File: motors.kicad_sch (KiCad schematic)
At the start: 5 parts, among them J11 Conn_01x03, J12 Conn_01x03, J13 Conn_01x03, J14 Conn_01x03, J15 Conn_01x03

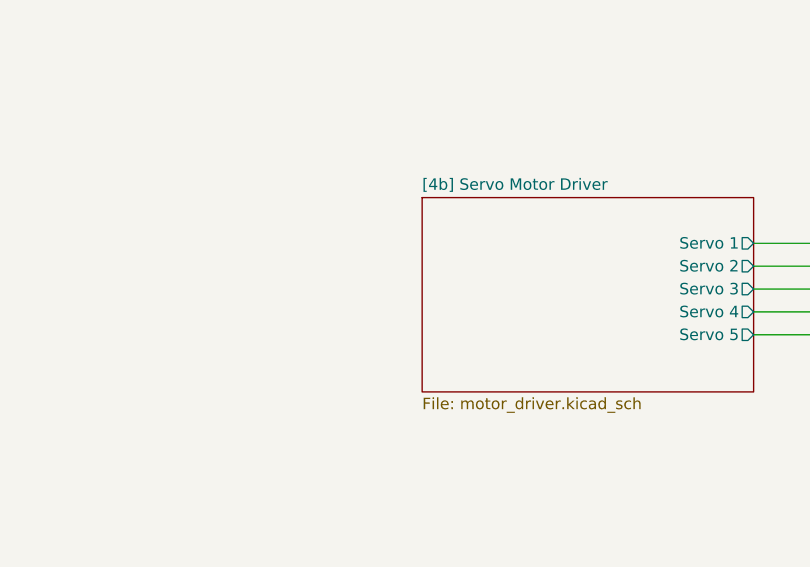
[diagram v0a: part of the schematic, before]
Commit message: feat(pcb): made the fan controlled by a NPN transistor
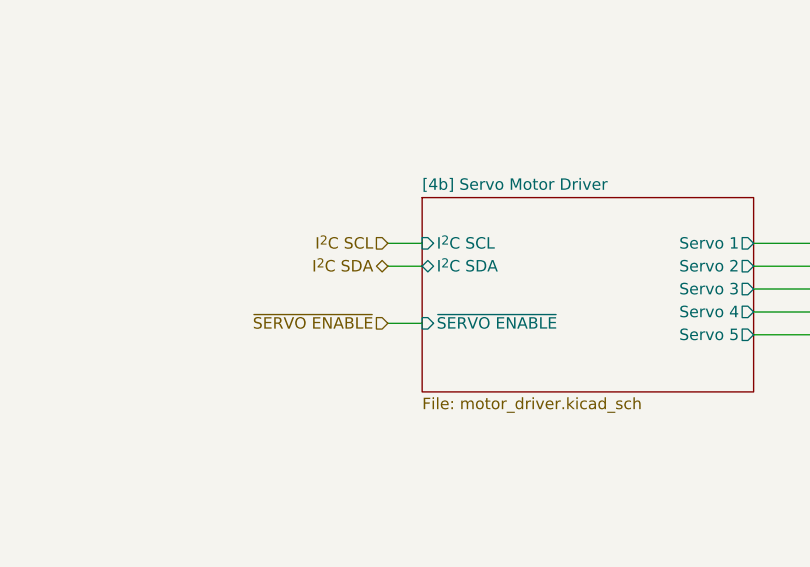
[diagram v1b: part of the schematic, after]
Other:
- sheet [4b] Servo Motor Driver ports: added I^{2}C SCL, I^{2}C SDA, ~{SERVO ENABLE}; removed none
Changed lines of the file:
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@@
+	(wire
+		(pts
+			(xy 165.1 80.01) (xy 168.91 80.01)
+		)
+		(stroke
+			(width 0)
+			(type default)
+		)
+	)
 	(wire
 		(pts
@@
 	(wire
 		(pts
+			(xy 165.1 82.55) (xy 168.91 82.55)
+		)
+		(stroke
+			(width 0)
+			(type default)
+		)
+	)
+	(wire
+		(pts
 			(xy 212.09 90.17) (xy 212.09 115.57)
 		)
@@
 		(pts
 			(xy 224.79 95.25) (xy 224.79 104.14)
+		)
+		(stroke
+			(width 0)
+			(type default)
+		)
+	)
+	(wire
+		(pts
+			(xy 165.1 88.9) (xy 168.91 88.9)
 		)
 		(stroke
@@
 		)
 	)
+	(hierarchical_label "I^{2}C SDA"
+		(shape bidirectional)
+		(at 165.1 82.55 180)
+		(effects
+			(font
+				(size 1.27 1.27)
+			)
+			(justify right)
+		)
+	)
 	(hierarchical_label "M2DB"
 		(shape input)
@@
 		)
 	)
+	(hierarchical_label "I^{2}C SCL"
+		(shape input)
+		(at 165.1 80.01 180)
+		(effects
+			(font
+				(size 1.27 1.27)
+			)
+			(justify right)
+		)
+	)
 	(hierarchical_label "M3DB"
 		(shape input)
@@
 		)
 	)
+	(hierarchical_label "~{SERVO ENABLE}"
+		(shape input)
+		(at 165.1 88.9 180)
+		(effects
+			(font
+				(size 1.27 1.27)
+			)
+			(justify right)
+		)
+	)
 	(rule_area
 		(polyline
 			(pts
-				(xy 247.65 67.31) (xy 166.37 67.31) (xy 166.37 128.27) (xy 247.65 128.27)
+				(xy 247.65 67.31) (xy 137.16 67.31) (xy 137.16 128.27) (xy 247.65 128.27)
 			)
 			(stroke
@@
 			)
 		)
+		(pin "I^{2}C SCL" input
+			(at 168.91 80.01 180)
+			(effects
+				(font
+					(size 1.27 1.27)
+				)
+				(justify left)
+			)
+		)
+		(pin "I^{2}C SDA" bidirectional
+			(at 168.91 82.55 180)
+			(effects
+				(font
+					(size 1.27 1.27)
+				)
+				(justify left)
+			)
+		)
+		(pin "~{SERVO ENABLE}" input
+			(at 168.91 88.9 180)
+			(effects
+				(font
+					(size 1.27 1.27)
+				)
+				(justify left)
+			)
+		)

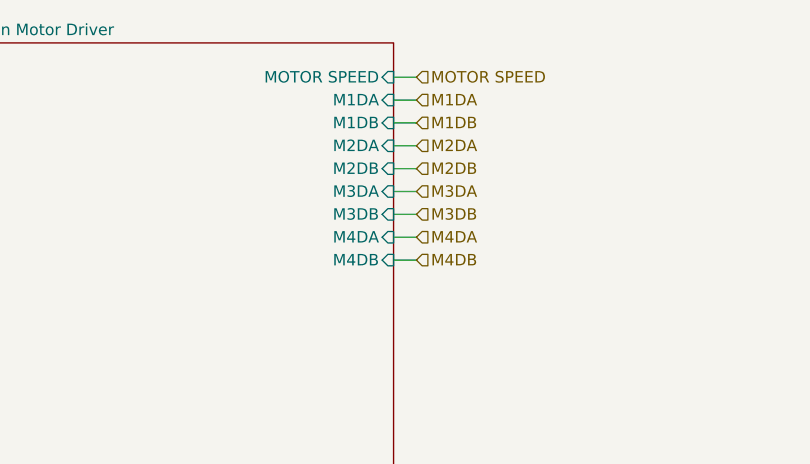
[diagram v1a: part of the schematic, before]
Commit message: doc(pcb): added docs for some of the main components of the HAT
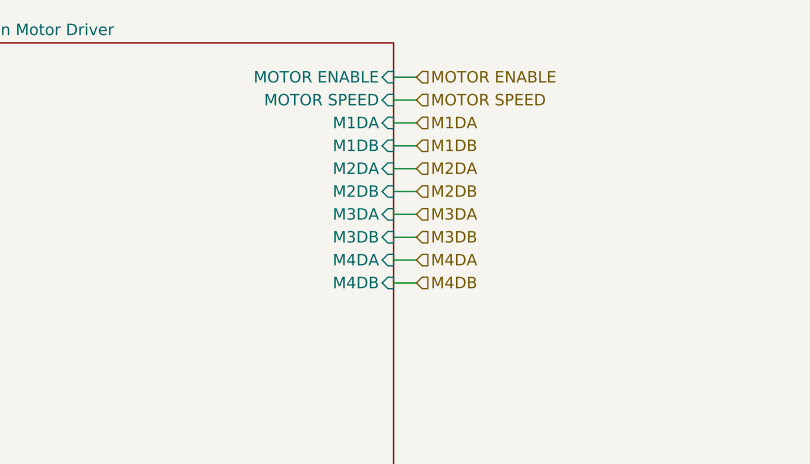
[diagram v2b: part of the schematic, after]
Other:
- sheet [4a] Main Motor Driver ports: added MOTOR ENABLE; removed none

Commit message: feat(pcb): (somewhat) finalized all the parts needed
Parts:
- J11, J12, J13, J14, J15: footprint (none) -> Connector_PinHeader_2.54mm:PinHeader_1x03_P2.54mm_Vertical
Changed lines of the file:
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@@
 			)
 		)
-		(property "Footprint" ""
+		(property "Footprint" "Connector_PinHeader_2.54mm:PinHeader_1x03_P2.54mm_Vertical"
 			(at 232.41 106.68 0)
 			(effects
@@
 			)
 		)
-		(property "Footprint" ""
+		(property "Footprint" "Connector_PinHeader_2.54mm:PinHeader_1x03_P2.54mm_Vertical"
 			(at 232.41 115.57 0)
 			(effects
@@
 			)
 		)
-		(property "Footprint" ""
+		(property "Footprint" "Connector_PinHeader_2.54mm:PinHeader_1x03_P2.54mm_Vertical"
 			(at 232.41 80.01 0)
 			(effects
@@
 			)
 		)
-		(property "Footprint" ""
+		(property "Footprint" "Connector_PinHeader_2.54mm:PinHeader_1x03_P2.54mm_Vertical"
 			(at 232.41 97.79 0)
 			(effects
@@
 			)
 		)
-		(property "Footprint" ""
+		(property "Footprint" "Connector_PinHeader_2.54mm:PinHeader_1x03_P2.54mm_Vertical"
 			(at 232.41 88.9 0)
 			(effects

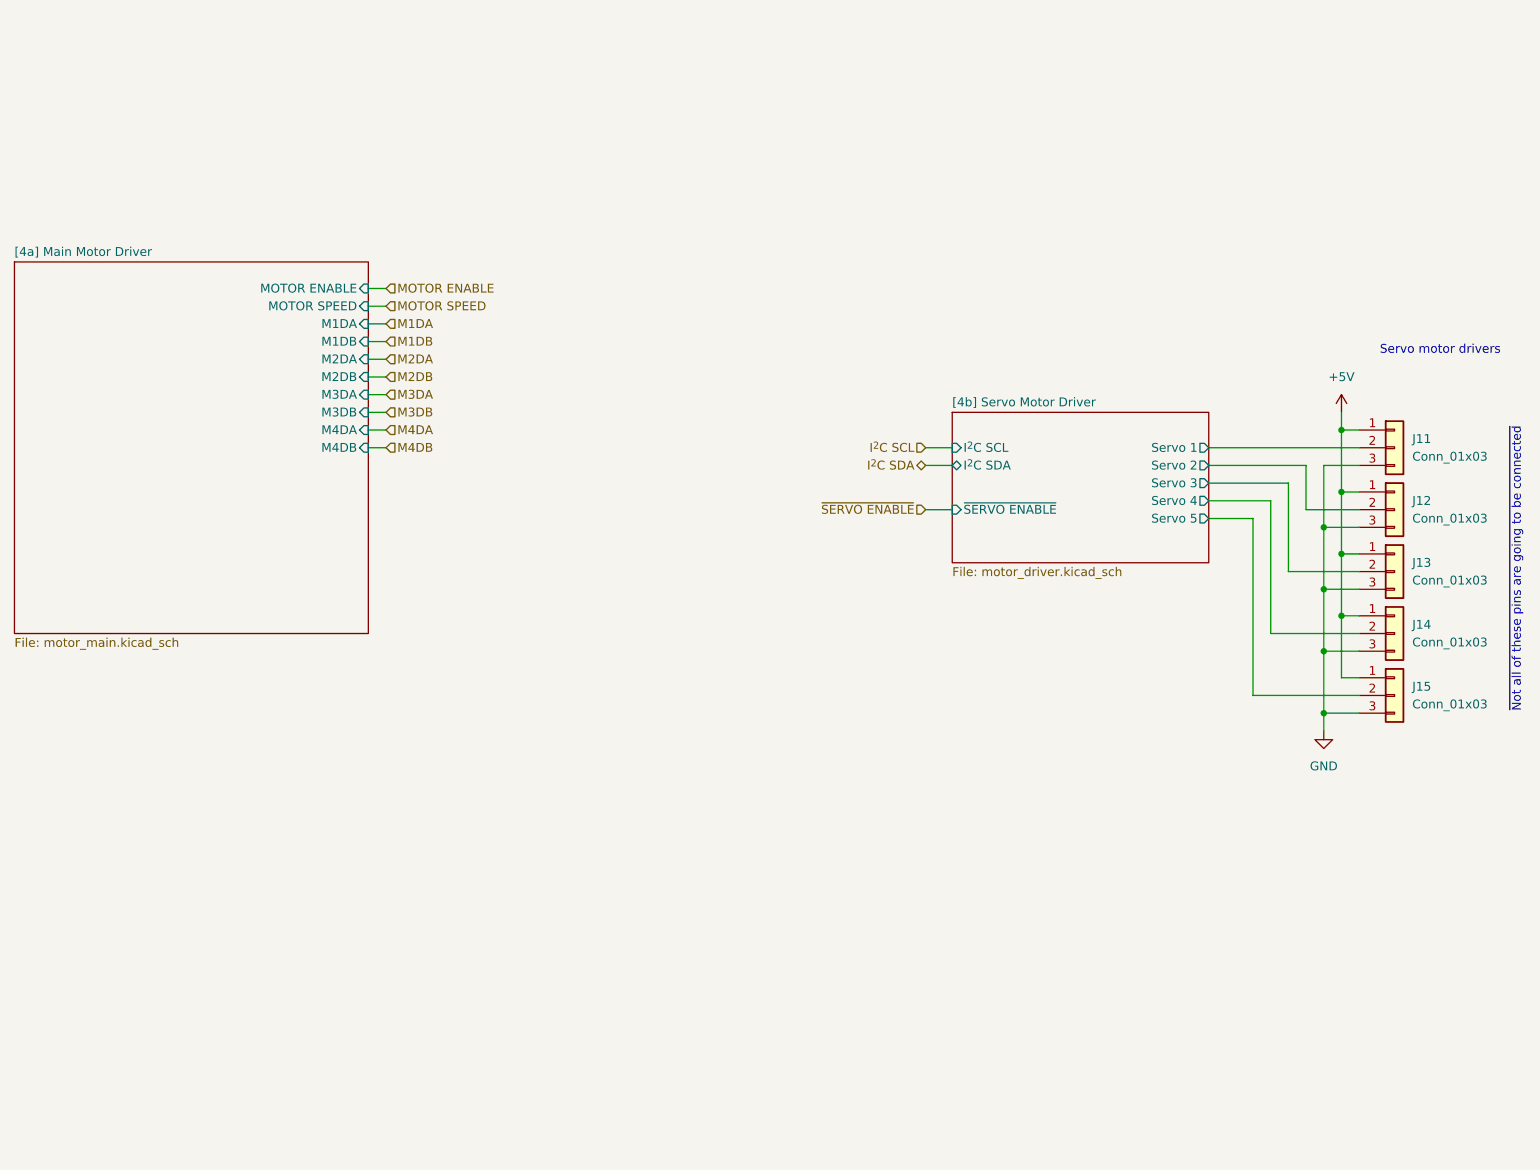
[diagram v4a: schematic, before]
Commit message: feat: removed servo motors
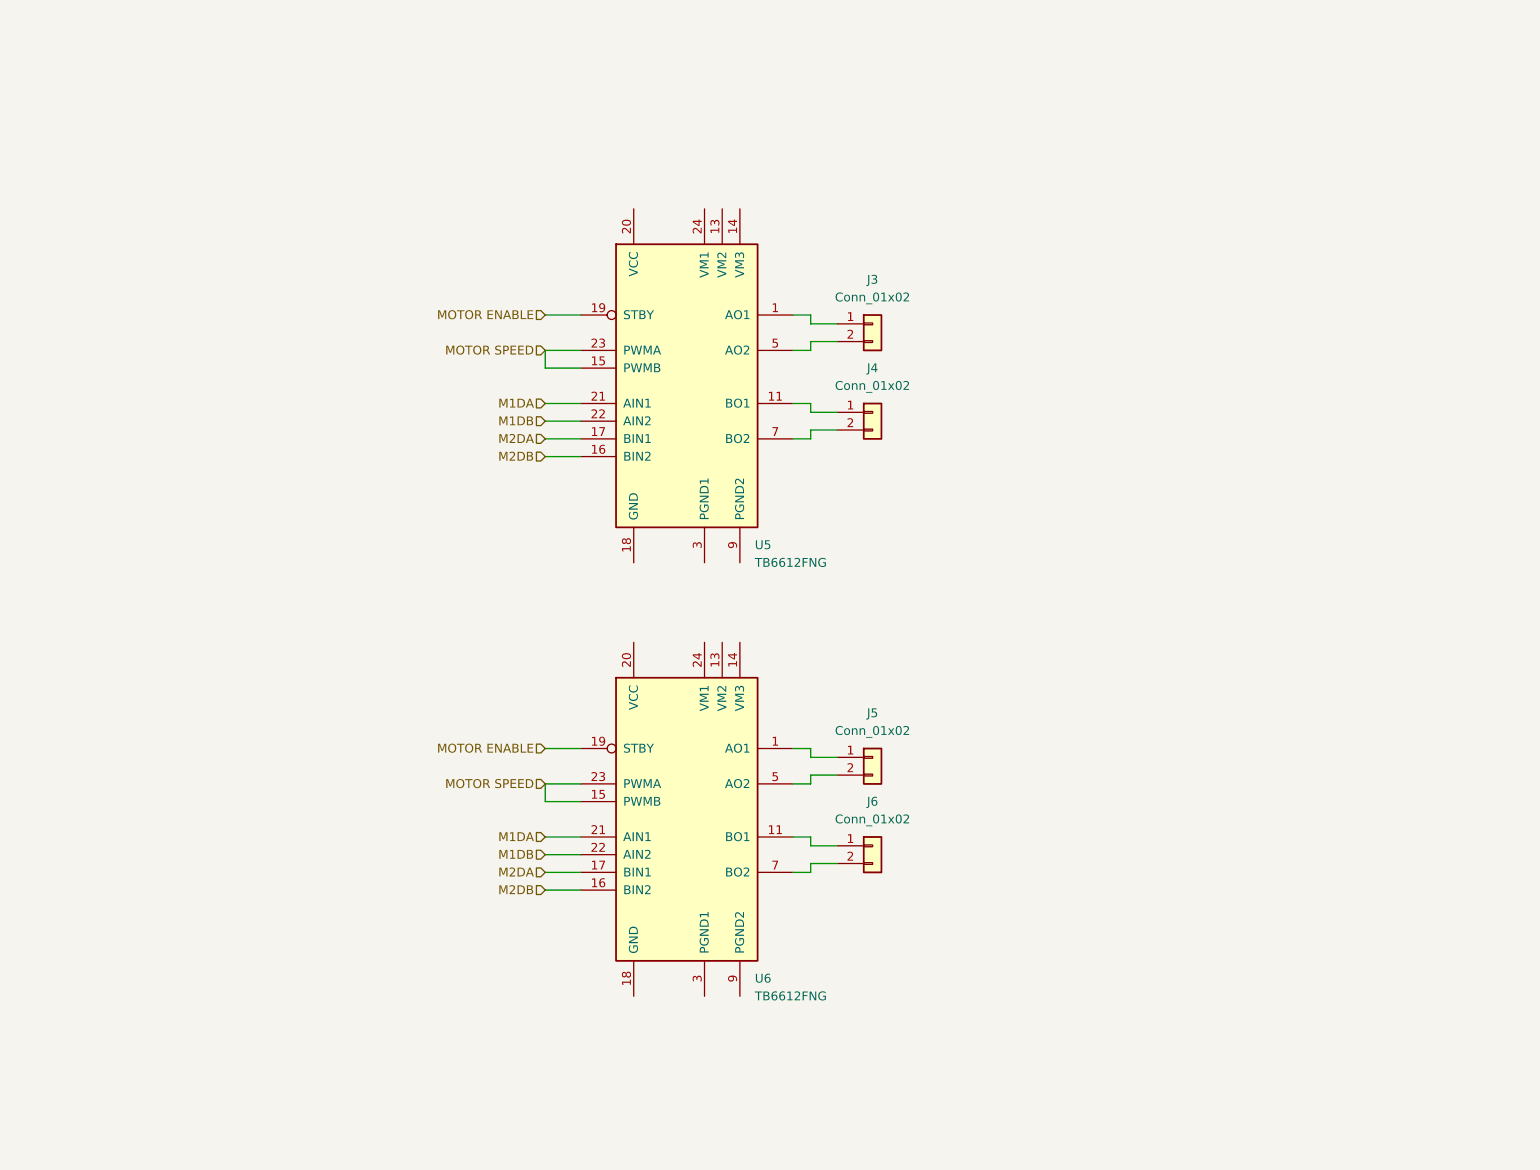
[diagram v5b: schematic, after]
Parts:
- removed J11, J12, J13, J14, J15: Conn_01x03, Connector_PinHeader_2.54mm:PinHeader_1x03_P2.54mm_Vertical, symbol Connector_Generic:Conn_01x03
- added J3, J4, J5, J6: Conn_01x02, Connector_PinHeader_2.54mm:PinHeader_1x02_P2.54mm_Vertical, symbol Connector_Generic:Conn_01x02
- added U5, U6: TB6612FNG, Package_SO:SSOP-24_5.3x8.2mm_P0.65mm, symbol Driver_Motor:TB6612FNG
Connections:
- net M1DA: now also U5.21 (AIN1), U6.21 (AIN1)
- net M1DB: now also U5.22 (AIN2), U6.22 (AIN2)
- net M2DA: now also U5.17 (BIN1), U6.17 (BIN1)
- net M2DB: now also U5.16 (BIN2), U6.16 (BIN2)
- net MOTOR ENABLE: now also U5.19 (STBY), U6.19 (STBY)
- net MOTOR SPEED: now also U5.15 (PWMB), U5.23 (PWMA), U6.15 (PWMB), U6.23 (PWMA)
- new net: J4.1 (Pin_1), U5.11 (BO1), U5.12 (BO1)
- new net: J4.2 (Pin_2), U5.7 (BO2), U5.8 (BO2)
- new net: J5.1 (Pin_1), U6.1 (AO1), U6.2 (AO1)
- new net: U6.10 (PGND2), U6.9 (PGND2)
- new net: J6.1 (Pin_1), U6.11 (BO1), U6.12 (BO1)
- new net: U6.3 (PGND1), U6.4 (PGND1)
- new net: J5.2 (Pin_2), U6.5 (AO2), U6.6 (AO2)
- new net: J6.2 (Pin_2), U6.7 (BO2), U6.8 (BO2)
- new net: J3.1 (Pin_1), U5.1 (AO1), U5.2 (AO1)
- new net: J3.2 (Pin_2), U5.5 (AO2), U5.6 (AO2)
- new net: U5.10 (PGND2), U5.9 (PGND2)
- new net: U5.3 (PGND1), U5.4 (PGND1)
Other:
- removed sheet [4a] Main Motor Driver
- removed sheet [4b] Servo Motor Driver
- note removed: "Servo motor drivers"
- note removed: "~{Not all of these pins are going to be connected}"

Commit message: feat: nets and stuff?? I guess?
I don't really remember what this commit changes
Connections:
- net MOTOR B1: now reaches J4.1 (Pin_1), U5.11 (BO1), U5.12 (BO1)
- net MOTOR B2: now reaches J4.2 (Pin_2), U5.7 (BO2), U5.8 (BO2)
- net MOTOR C1: now reaches J5.1 (Pin_1), U6.1 (AO1), U6.2 (AO1)
- net MOTOR D1: now reaches J6.1 (Pin_1), U6.11 (BO1), U6.12 (BO1)
- net MOTOR C2: now reaches J5.2 (Pin_2), U6.5 (AO2), U6.6 (AO2)
- net MOTOR D2: now reaches J6.2 (Pin_2), U6.7 (BO2), U6.8 (BO2)
- net MOTOR A1: now reaches J3.1 (Pin_1), U5.1 (AO1), U5.2 (AO1)
- net MOTOR A2: now reaches J3.2 (Pin_2), U5.5 (AO2), U5.6 (AO2)
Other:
- moved on the sheet: J3, J4, J5, J6
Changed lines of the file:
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@@
 	(wire
 		(pts
-			(xy 152.4 139.7) (xy 148.59 139.7)
+			(xy 163.83 139.7) (xy 148.59 139.7)
 		)
 		(stroke
@@
 	(wire
 		(pts
-			(xy 152.4 127) (xy 148.59 127)
+			(xy 163.83 127) (xy 148.59 127)
 		)
 		(stroke
@@
 	(wire
 		(pts
-			(xy 152.4 77.47) (xy 148.59 77.47)
+			(xy 163.83 77.47) (xy 148.59 77.47)
 		)
 		(stroke
@@
 	(wire
 		(pts
-			(xy 148.59 62.23) (xy 152.4 62.23)
-		)
-		(stroke
-			(width 0)
-			(type default)
-		)
-	)
-	(wire
-		(pts
-			(xy 148.59 135.89) (xy 148.59 137.16)
+			(xy 148.59 62.23) (xy 163.83 62.23)
+		)
+		(stroke
+			(width 0)
+			(type default)
+		)
+	)
+	(wire
+		(pts
+			(xy 148.59 137.16) (xy 148.59 135.89)
 		)
 		(stroke
@@
 	(wire
 		(pts
-			(xy 148.59 124.46) (xy 152.4 124.46)
+			(xy 148.59 124.46) (xy 163.83 124.46)
 		)
 		(stroke
@@
 	(wire
 		(pts
-			(xy 148.59 73.66) (xy 148.59 74.93)
+			(xy 148.59 74.93) (xy 148.59 73.66)
 		)
 		(stroke
@@
 	(wire
 		(pts
-			(xy 152.4 64.77) (xy 148.59 64.77)
+			(xy 163.83 64.77) (xy 148.59 64.77)
 		)
 		(stroke
@@
 	(wire
 		(pts
-			(xy 148.59 74.93) (xy 152.4 74.93)
+			(xy 148.59 74.93) (xy 163.83 74.93)
 		)
 		(stroke
@@
 	(wire
 		(pts
-			(xy 148.59 123.19) (xy 148.59 124.46)
-		)
-		(stroke
-			(width 0)
-			(type default)
-		)
-	)
-	(wire
-		(pts
-			(xy 148.59 137.16) (xy 152.4 137.16)
-		)
-		(stroke
-			(width 0)
-			(type default)
+			(xy 148.59 124.46) (xy 148.59 123.19)
+		)
+		(stroke
+			(width 0)
+			(type default)
+		)
+	)
+	(wire
+		(pts
+			(xy 148.59 137.16) (xy 163.83 137.16)
+		)
+		(stroke
+			(width 0)
+			(type default)
+		)
+	)
+	(label "MOTOR B1"
+		(at 152.4 74.93 0)
+		(effects
+			(font
+				(size 1.27 1.27)
+			)
+			(justify left bottom)
+		)
+	)
+	(label "MOTOR D1"
+		(at 152.4 137.16 0)
+		(effects
+			(font
+				(size 1.27 1.27)
+			)
+			(justify left bottom)
+		)
+	)
+	(label "MOTOR C2"
+		(at 152.4 127 0)
+		(effects
+			(font
+				(size 1.27 1.27)
+			)
+			(justify left bottom)
+		)
+	)
+	(label "MOTOR C1"
+		(at 152.4 124.46 0)
+		(effects
+			(font
+				(size 1.27 1.27)
+			)
+			(justify left bottom)
+		)
+	)
+	(label "MOTOR A1"
+		(at 152.4 62.23 0)
+		(effects
+			(font
+				(size 1.27 1.27)
+			)
+			(justify left bottom)
+		)
+	)
+	(label "MOTOR B2"
+		(at 152.4 77.47 0)
+		(effects
+			(font
+				(size 1.27 1.27)
+			)
+			(justify left bottom)
+		)
+	)
+	(label "MOTOR D2"
+		(at 152.4 139.7 0)
+		(effects
+			(font
+				(size 1.27 1.27)
+			)
+			(justify left bottom)
+		)
+	)
+	(label "MOTOR A2"
+		(at 152.4 64.77 0)
+		(effects
+			(font
+				(size 1.27 1.27)
+			)
+			(justify left bottom)
 		)
 	)
@@
 	(symbol
 		(lib_id "Connector_Generic:Conn_01x02")
-		(at 157.48 74.93 0)
+		(at 168.91 74.93 0)
 		(unit 1)
 		(exclude_from_sim no)
@@
 		(dnp no)
 		(property "Reference" "J4"
-			(at 157.48 68.58 0)
+			(at 168.91 68.58 0)
 			(effects
 				(font
@@
 		)
 		(property "Value" "Conn_01x02"
-			(at 157.48 71.12 0)
+			(at 168.91 71.12 0)
 			(effects
 				(font
@@
 		)
 		(property "Footprint" "Connector_PinHeader_2.54mm:PinHeader_1x02_P2.54mm_Vertical"
-			(at 157.48 74.93 0)
+			(at 168.91 74.93 0)
 			(effects
 				(font
@@
 		)
 		(property "Datasheet" "~"
-			(at 157.48 74.93 0)
+			(at 168.91 74.93 0)
 			(effects
 				(font
@@
 		)
 		(property "Description" "Generic connector, single row, 01x02, script generated (kicad-library-utils/schlib/autogen/connector/)"
-			(at 157.48 74.93 0)
+			(at 168.91 74.93 0)
 			(effects
 				(font
@@
 	(symbol
 		(lib_id "Connector_Generic:Conn_01x02")
-		(at 157.48 62.23 0)
+		(at 168.91 62.23 0)
 		(unit 1)
 		(exclude_from_sim no)
@@
 		(dnp no)
 		(property "Reference" "J3"
-			(at 157.48 55.88 0)
+			(at 168.91 55.88 0)
 			(effects
 				(font
@@
 		)
 		(property "Value" "Conn_01x02"
-			(at 157.48 58.42 0)
+			(at 168.91 58.42 0)
 			(effects
 				(font
@@
 		)
 		(property "Footprint" "Connector_PinHeader_2.54mm:PinHeader_1x02_P2.54mm_Vertical"
-			(at 157.48 62.23 0)
+			(at 168.91 62.23 0)
 			(effects
 				(font
@@
 		)
 		(property "Datasheet" "~"
-			(at 157.48 62.23 0)
+			(at 168.91 62.23 0)
 			(effects
 				(font
@@
 		)
 		(property "Description" "Generic connector, single row, 01x02, script generated (kicad-library-utils/schlib/autogen/connector/)"
-			(at 157.48 62.23 0)
+			(at 168.91 62.23 0)
 			(effects
 				(font
@@
 	(symbol
 		(lib_id "Connector_Generic:Conn_01x02")
-		(at 157.48 137.16 0)
+		(at 168.91 137.16 0)
 		(unit 1)
 		(exclude_from_sim no)
@@
 		(dnp no)
 		(property "Reference" "J6"
-			(at 157.48 130.81 0)
+			(at 168.91 130.81 0)
 			(effects
 				(font
@@
 		)
 		(property "Value" "Conn_01x02"
-			(at 157.48 133.35 0)
+			(at 168.91 133.35 0)
 			(effects
 				(font
@@
 		)
 		(property "Footprint" "Connector_PinHeader_2.54mm:PinHeader_1x02_P2.54mm_Vertical"
-			(at 157.48 137.16 0)
+			(at 168.91 137.16 0)
 			(effects
 				(font
@@
 		)
 		(property "Datasheet" "~"
-			(at 157.48 137.16 0)
+			(at 168.91 137.16 0)
 			(effects
 				(font
@@
 		)
 		(property "Description" "Generic connector, single row, 01x02, script generated (kicad-library-utils/schlib/autogen/connector/)"
-			(at 157.48 137.16 0)
+			(at 168.91 137.16 0)
 			(effects
 				(font
@@
 	(symbol
 		(lib_id "Connector_Generic:Conn_01x02")
-		(at 157.48 124.46 0)
+		(at 168.91 124.46 0)
 		(unit 1)
 		(exclude_from_sim no)
@@
 		(dnp no)
 		(property "Reference" "J5"
-			(at 157.48 118.11 0)
+			(at 168.91 118.11 0)
 			(effects
 				(font
@@
 		)
 		(property "Value" "Conn_01x02"
-			(at 157.48 120.65 0)
+			(at 168.91 120.65 0)
 			(effects
 				(font
@@
 		)
 		(property "Footprint" "Connector_PinHeader_2.54mm:PinHeader_1x02_P2.54mm_Vertical"
-			(at 157.48 124.46 0)
+			(at 168.91 124.46 0)
 			(effects
 				(font
@@
 		)
 		(property "Datasheet" "~"
-			(at 157.48 124.46 0)
+			(at 168.91 124.46 0)
 			(effects
 				(font
@@
 		)
 		(property "Description" "Generic connector, single row, 01x02, script generated (kicad-library-utils/schlib/autogen/connector/)"
-			(at 157.48 124.46 0)
-			(effects
-				(font
+			(at 168.91 124.46 0)
+			(effects
+				(font
